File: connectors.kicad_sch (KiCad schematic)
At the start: 45 parts, among them J10 USB-C_GCT_USB4145-03-0070-C, J8 10107844-002LF, J9 JST_XH_1x2_B2B-XH-A-LF-SN, Q29 BC807-25W, SW1 MSS3-V-T_R

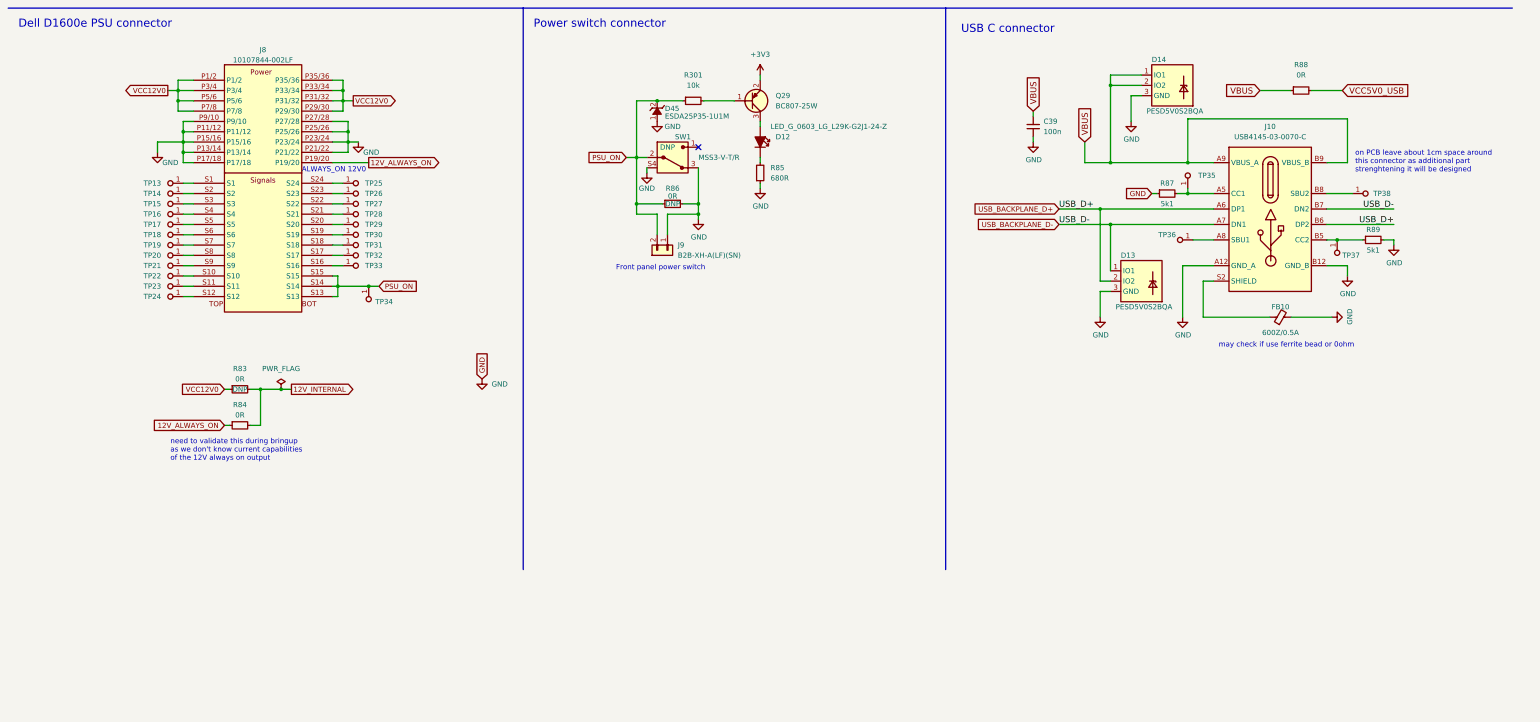
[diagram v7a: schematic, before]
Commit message: Cleaning ERC on schematic
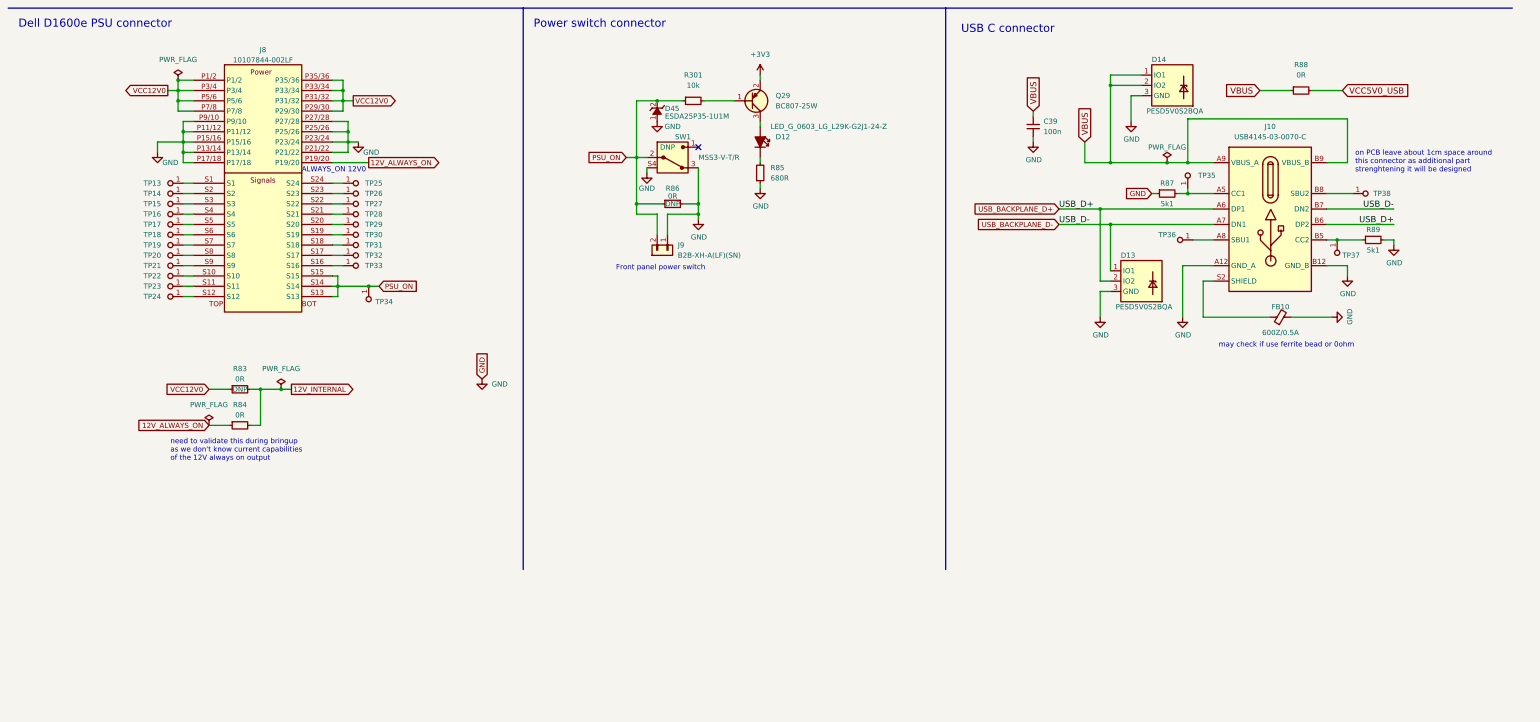
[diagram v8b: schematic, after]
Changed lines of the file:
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@@
   (junction (at 115.57 82.55) (diameter 0) (color 0 0 0 0)
   )
+  (junction (at 74.93 77.47) (diameter 0) (color 0 0 0 0)
+  )
   (junction (at 76.2 90.17) (diameter 0) (color 0 0 0 0)
   )
@@
   (junction (at 116.84 92.71) (diameter 0) (color 0 0 0 0)
   )
+  (junction (at 318.77 97.79) (diameter 0) (color 0 0 0 0)
+  )
   (junction (at 187.96 96.52) (diameter 0) (color 0 0 0 0)
   )
@@
     (stroke (width 0) (type default) (color 0 0 0 0))
   )
-  (wire (pts (xy 86.36 162.56) (xy 87.63 162.56))
-    (stroke (width 0) (type default) (color 0 0 0 0))
-  )
   (wire (pts (xy 372.11 116.84) (xy 374.65 116.84))
     (stroke (width 0) (type default) (color 0 0 0 0))
@@
     (stroke (width 0) (type default) (color 0 0 0 0))
   )
+  (wire (pts (xy 318.77 97.79) (xy 323.85 97.79))
+    (stroke (width 0) (type default) (color 0 0 0 0))
+  )
   (wire (pts (xy 309.88 87.63) (xy 309.88 81.28))
     (stroke (width 0) (type default) (color 0 0 0 0))
@@
     (stroke (width 0) (type default) (color 0 0 0 0))
   )
-  (wire (pts (xy 86.36 153.67) (xy 87.63 153.67))
+  (wire (pts (xy 82.55 153.67) (xy 87.63 153.67))
     (stroke (width 0) (type default) (color 0 0 0 0))
   )
@@
     (stroke (width 0) (type default) (color 0 0 0 0))
   )
-  (wire (pts (xy 304.8 97.79) (xy 323.85 97.79))
+  (wire (pts (xy 304.8 97.79) (xy 318.77 97.79))
     (stroke (width 0) (type default) (color 0 0 0 0))
   )
@@
     (stroke (width 0) (type default) (color 0 0 0 0))
   )
+  (wire (pts (xy 82.55 162.56) (xy 87.63 162.56))
+    (stroke (width 0) (type default) (color 0 0 0 0))
+  )
   (wire (pts (xy 119.38 92.71) (xy 116.84 92.71))
     (stroke (width 0) (type default) (color 0 0 0 0))
@@
     )
   )
-  (global_label "VCC12V0" (shape input) (at 86.36 153.67 180) (fields_autoplaced)
+  (global_label "VCC12V0" (shape input) (at 82.55 153.67 180) (fields_autoplaced)
     (effects (font (size 1.27 1.27)) (justify right))
-    (property "Intersheet References" "${INTERSHEET_REFS}" (id 0) (at 75.6901 153.7494 0)
+    (property "Intersheet References" "${INTERSHEET_REFS}" (id 0) (at 71.8801 153.7494 0)
       (effects (font (size 1.27 1.27)) (justify right) hide)
     )
@@
     )
   )
-  (global_label "12V_ALWAYS_ON" (shape input) (at 86.36 162.56 180) (fields_autoplaced)
+  (global_label "12V_ALWAYS_ON" (shape input) (at 82.55 162.56 180) (fields_autoplaced)
     (effects (font (size 1.27 1.27)) (justify right))
-    (property "Intersheet References" "${INTERSHEET_REFS}" (id 0) (at 68.9772 162.4806 0)
+    (property "Intersheet References" "${INTERSHEET_REFS}" (id 0) (at 65.1672 162.4806 0)
       (effects (font (size 1.27 1.27)) (justify right) hide)
     )
@@
     (pin "1")
   )
+  (symbol (lib_id "antmicropower:PWR_FLAG") (at 74.93 77.47 0) (unit 1)
+    (in_bom yes) (on_board yes) (fields_autoplaced)
+    (property "Reference" "#FLG0109" (id 0) (at 74.93 75.565 0)
+      (effects (font (size 1.27 1.27)) hide)
+    )
+    (property "Value" "PWR_FLAG" (id 1) (at 74.93 72.39 0))
+    (property "Footprint" "" (id 2) (at 74.93 77.47 0)
+      (effects (font (size 1.27 1.27)) hide)
+    )
+    (property "Datasheet" "" (id 3) (at 74.93 77.47 0)
+      (effects (font (size 1.27 1.27)) hide)
+    )
+    (pin "1")
+  )
   (symbol (lib_id "antmicropower:GND") (at 193.04 87.63 0) (unit 1)
     (in_bom yes) (on_board yes)
@@
     (pin "1")
   )
+  (symbol (lib_id "antmicropower:PWR_FLAG") (at 318.77 97.79 0) (unit 1)
+    (in_bom yes) (on_board yes)
+    (property "Reference" "#FLG0111" (id 0) (at 318.77 95.885 0)
+      (effects (font (size 1.27 1.27)) hide)
+    )
+    (property "Value" "PWR_FLAG" (id 1) (at 318.77 93.98 0))
+    (property "Footprint" "" (id 2) (at 318.77 97.79 0)
+      (effects (font (size 1.27 1.27)) hide)
+    )
+    (property "Datasheet" "" (id 3) (at 318.77 97.79 0)
+      (effects (font (size 1.27 1.27)) hide)
+    )
+    (pin "1")
+  )
   (symbol (lib_id "antmicroWire2BoardConnectors:JST_XH_1x2_B2B-XH-A-LF-SN") (at 195.58 115.57 270) (unit 1)
     (in_bom yes) (on_board yes) (fields_autoplaced)
@@
       (effects (font (size 1.27 1.27)) hide)
     )
+    (pin "1")
+  )
+  (symbol (lib_id "antmicropower:PWR_FLAG") (at 82.55 162.56 0) (unit 1)
+    (in_bom yes) (on_board yes) (fields_autoplaced)
+    (property "Reference" "#FLG0110" (id 0) (at 82.55 160.655 0)
+      (effects (font (size 1.27 1.27)) hide)
+    )
+    (property "Value" "PWR_FLAG" (id 1) (at 82.55 157.48 0))
+    (property "Footprint" "" (id 2) (at 82.55 162.56 0)
+      (effects (font (size 1.27 1.27)) hide)
+    )
+    (property "Datasheet" "" (id 3) (at 82.55 162.56 0)
+      (effects (font (size 1.27 1.27)) hide)
+    )
